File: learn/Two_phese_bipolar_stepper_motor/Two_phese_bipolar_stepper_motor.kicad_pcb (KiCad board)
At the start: 2 copper layers, 73.7 x 81 mm, 25 parts, among them J1 Screw_Terminal_01x02, J2 Screw_Terminal_01x02, J3 Screw_Terminal_01x12, J4 Screw_Terminal_01x04, U1 L297, U2 L298N

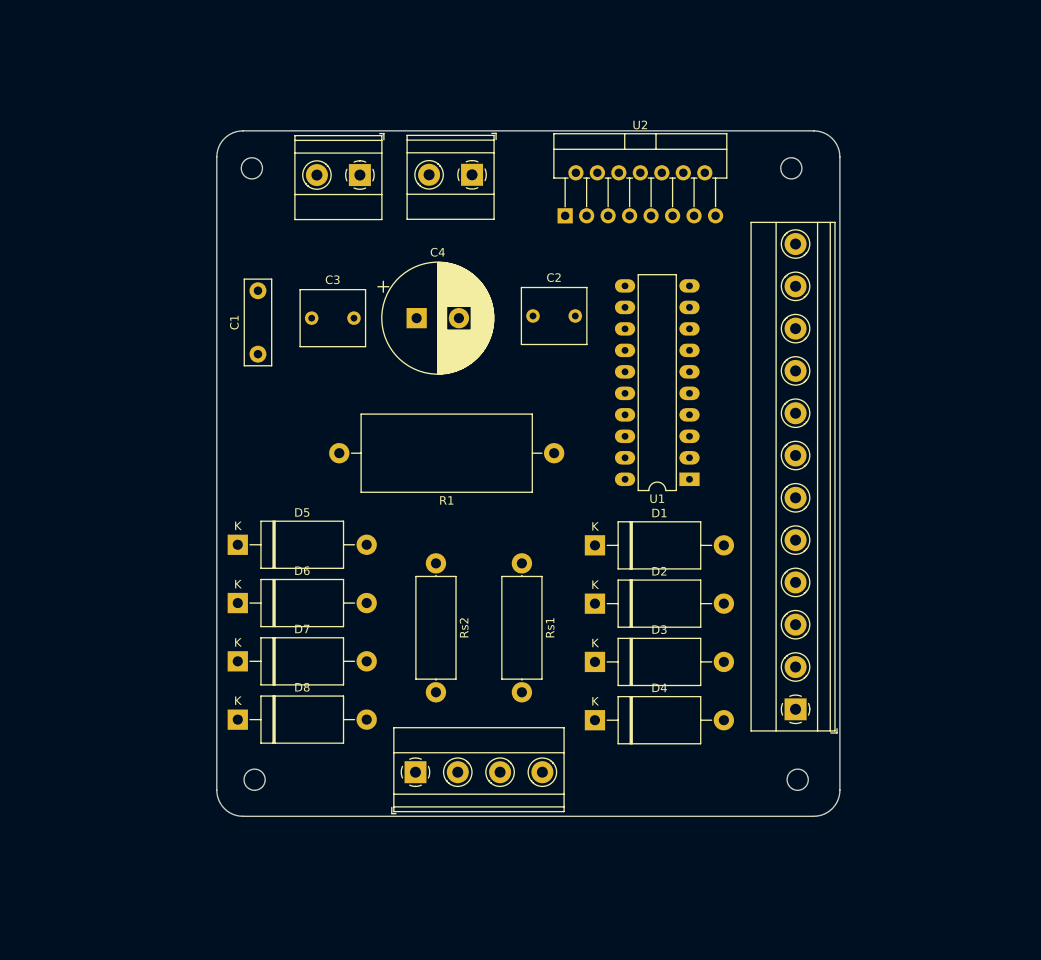
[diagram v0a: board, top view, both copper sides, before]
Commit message: Two_phase: print the wire
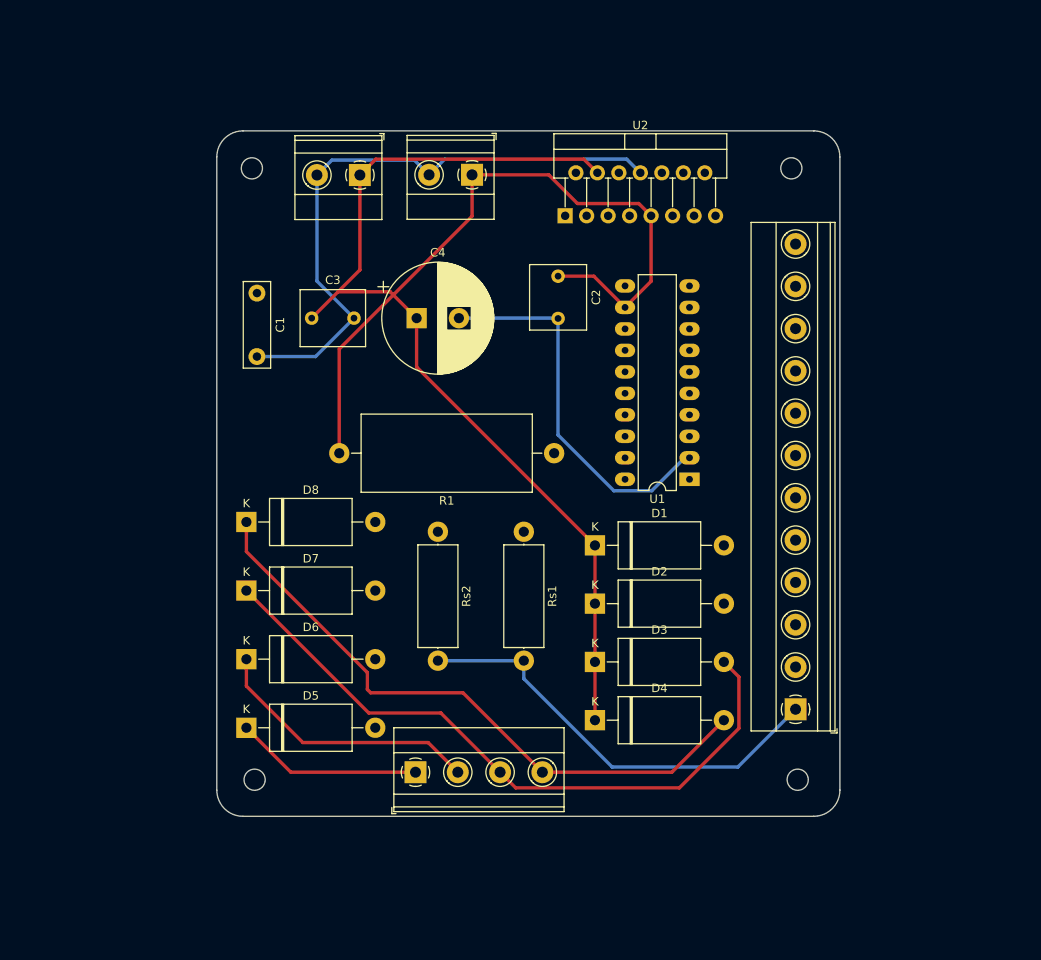
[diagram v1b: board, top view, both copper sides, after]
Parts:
- moved D8 23.4 mm to (116.5, 98.6)
- moved D5 21.7 mm to (116.5, 122.9)
- moved D7 8.42 mm to (116.5, 106.7)
- moved C1 7.22 mm to (117.8, 71.5), turned to -90 degrees
- moved D6 6.71 mm to (116.5, 114.8)
- moved C2 5.56 mm to (153.4, 69.5), turned to -90 degrees
- moved Rs2 3.74 mm to (139.2, 99.7)
- moved Rs1 3.74 mm to (149.3, 99.7)
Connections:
- C2 pad 1: VSS -> VS
- J2 pad 1: VSS -> VS
- R1 pad 2: VSS -> VS
- U1 pad 12: VSS -> VS
- U2 pad 9: VSS -> VS
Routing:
- net VS: track 0.00 -> 199.8 mm
- net GND: track 0.00 -> 170.7 mm
- net Net-(D3-A): track 0.00 -> 79.4 mm
- net Net-(D4-A): track 0.00 -> 74.5 mm
- net Net-(D2-A): track 0.00 -> 32.4 mm
- net Net-(D1-A): track 0.00 -> 22.2 mm

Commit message: two_phase: made pcb
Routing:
- net /OSC: track 0.00 -> 99.6 mm, vias 0 -> 1
- net Net-(D1-A): track 22.2 -> 93.1 mm
- net Net-(D2-A): track 32.4 -> 89.6 mm
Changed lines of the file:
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@@
   (gr_line (start 113.029957 55.410043) (end 113.029957 130.26)
     (stroke (width 0.1) (type default)) (layer "Edge.Cuts"))
+  (segment (start 128.2 93.975) (end 146.875 93.975) (width 0.4) (layer "F.Cu") (net 1))
+  (segment (start 117.775 71.5) (end 116.225 73.05) (width 0.4) (layer "F.Cu") (net 1))
+  (segment (start 116.225 73.05) (end 116.225 82) (width 0.4) (layer "F.Cu") (net 1))
+  (segment (start 152.908 90.424) (end 159.982 83.35) (width 0.4) (layer "F.Cu") (net 1))
+  (segment (start 174.325 68.575) (end 167.825 68.575) (width 0.4) (layer "F.Cu") (net 1))
+  (segment (start 163.04 81.6) (end 161.29 83.35) (width 0.4) (layer "F.Cu") (net 1))
+  (segment (start 167.825 68.575) (end 163.04 73.36) (width 0.4) (layer "F.Cu") (net 1))
+  (segment (start 163.04 73.36) (end 163.04 81.6) (width 0.4) (layer "F.Cu") (net 1))
+  (segment (start 181.45 75.7) (end 174.325 68.575) (width 0.4) (layer "F.Cu") (net 1))
+  (segment (start 159.982 83.35) (end 161.29 83.35) (width 0.4) (layer "F.Cu") (net 1))
+  (segment (start 116.225 82) (end 128.2 93.975) (width 0.4) (layer "F.Cu") (net 1))
+  (via (at 146.875 93.975) (size 0.8) (drill 0.4) (layers "F.Cu" "B.Cu") (net 1))
+  (segment (start 149.357 93.975) (end 152.908 90.424) (width 0.4) (layer "B.Cu") (net 1))
+  (segment (start 146.875 93.975) (end 149.357 93.975) (width 0.4) (layer "B.Cu") (net 1))
   (segment (start 159.769 127.525) (end 174.625 127.525) (width 0.4) (layer "B.Cu") (net 2))
   (segment (start 141.652 74.46) (end 153.335 74.46) (width 0.4) (layer "B.Cu") (net 2))
@@
   (segment (start 143.205 62.410189) (end 127.508 78.107189) (width 0.4) (layer "F.Cu") (net 3))
   (segment (start 121.778666 128.137) (end 116.525 122.883334) (width 0.4) (layer "F.Cu") (net 4))
+  (segment (start 176.925 125.73566) (end 176.925 105.271) (width 0.4) (layer "F.Cu") (net 4))
+  (segment (start 140.756 132.375) (end 170.28566 132.375) (width 0.4) (layer "F.Cu") (net 4))
+  (segment (start 170.28566 132.375) (end 176.925 125.73566) (width 0.4) (layer "F.Cu") (net 4))
+  (segment (start 136.518 128.137) (end 140.756 132.375) (width 0.4) (layer "F.Cu") (net 4))
+  (segment (start 176.925 105.271) (end 172.974 101.32) (width 0.4) (layer "F.Cu") (net 4))
   (segment (start 136.518 128.137) (end 121.778666 128.137) (width 0.4) (layer "F.Cu") (net 4))
   (segment (start 138.014334 124.633334) (end 123.208334 124.633334) (width 0.4) (layer "F.Cu") (net 5))
+  (segment (start 169.975 131.625) (end 145.006 131.625) (width 0.4) (layer "F.Cu") (net 5))
+  (segment (start 172.974 108.21) (end 176.175 111.411) (width 0.4) (layer "F.Cu") (net 5))
   (segment (start 116.525 117.95) (end 116.525 114.775) (width 0.4) (layer "F.Cu") (net 5))
   (segment (start 141.518 128.137) (end 138.014334 124.633334) (width 0.4) (layer "F.Cu") (net 5))
+  (segment (start 176.175 111.411) (end 176.175 125.425) (width 0.4) (layer "F.Cu") (net 5))
+  (segment (start 145.006 131.625) (end 141.518 128.137) (width 0.4) (layer "F.Cu") (net 5))
+  (segment (start 176.175 125.425) (end 169.975 131.625) (width 0.4) (layer "F.Cu") (net 5))
   (segment (start 123.208334 124.633334) (end 116.525 117.95) (width 0.4) (layer "F.Cu") (net 5))
   (segment (start 167.713 129.987) (end 174.75 122.95) (width 0.4) (layer "F.Cu") (net 6))

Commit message: two_phase: made a pcb
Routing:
- net Net-(D3-A): track 79.4 -> 166.0 mm, vias 0 -> 1
- net Net-(D2-A): track 89.6 -> 149.7 mm
- net /Rs2: track 0.00 -> 34.3 mm, vias 0 -> 1
- net /Rs1: track 0.00 -> 30.6 mm, vias 0 -> 1
- net GND: track 170.7 -> 184.6 mm
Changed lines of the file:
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@@
   (segment (start 159.769 127.525) (end 174.625 127.525) (width 0.4) (layer "B.Cu") (net 2))
   (segment (start 141.652 74.46) (end 153.335 74.46) (width 0.4) (layer "B.Cu") (net 2))
+  (segment (start 130.996 72.71) (end 139.902 72.71) (width 0.4) (layer "B.Cu") (net 2))
   (segment (start 136.39 55.78) (end 126.63 55.78) (width 0.4) (layer "B.Cu") (net 2))
   (segment (start 161.485 55.665) (end 163.1 57.28) (width 0.4) (layer "B.Cu") (net 2))
@@
   (segment (start 149.325 117.081) (end 159.769 127.525) (width 0.4) (layer "B.Cu") (net 2))
   (segment (start 168.35 90.97) (end 168.91 90.97) (width 0.4) (layer "B.Cu") (net 2))
+  (segment (start 139.902 72.71) (end 141.652 74.46) (width 0.4) (layer "B.Cu") (net 2))
   (segment (start 159.96 94.86) (end 164.46 94.86) (width 0.4) (layer "B.Cu") (net 2))
   (segment (start 138.125 57.515) (end 136.39 55.78) (width 0.4) (layer "B.Cu") (net 2))
@@
   (segment (start 129.246 74.46) (end 124.706 79) (width 0.4) (layer "B.Cu") (net 2))
   (segment (start 126.63 55.78) (end 124.865 57.545) (width 0.4) (layer "B.Cu") (net 2))
+  (segment (start 129.246 74.46) (end 130.996 72.71) (width 0.4) (layer "B.Cu") (net 2))
   (segment (start 127.508 78.107189) (end 127.508 90.424) (width 0.4) (layer "F.Cu") (net 3))
   (segment (start 131.825 55.665) (end 156.405 55.665) (width 0.4) (layer "F.Cu") (net 3))
@@
   (segment (start 138.014334 124.633334) (end 123.208334 124.633334) (width 0.4) (layer "F.Cu") (net 5))
   (segment (start 169.975 131.625) (end 145.006 131.625) (width 0.4) (layer "F.Cu") (net 5))
+  (segment (start 151.158 91.383) (end 151.158 69.67139) (width 0.4) (layer "F.Cu") (net 5))
+  (segment (start 159.914 95.15) (end 154.925 95.15) (width 0.4) (layer "F.Cu") (net 5))
+  (segment (start 172.974 108.21) (end 159.914 95.15) (width 0.4) (layer "F.Cu") (net 5))
+  (segment (start 154.925 95.15) (end 151.158 91.383) (width 0.4) (layer "F.Cu") (net 5))
+  (segment (start 151.158 69.67139) (end 156.75 64.07939) (width 0.4) (layer "F.Cu") (net 5))
   (segment (start 172.974 108.21) (end 176.175 111.411) (width 0.4) (layer "F.Cu") (net 5))
   (segment (start 116.525 117.95) (end 116.525 114.775) (width 0.4) (layer "F.Cu") (net 5))
   (segment (start 141.518 128.137) (end 138.014334 124.633334) (width 0.4) (layer "F.Cu") (net 5))
   (segment (start 176.175 111.411) (end 176.175 125.425) (width 0.4) (layer "F.Cu") (net 5))
+  (segment (start 156.75 64.07939) (end 156.75 62.36) (width 0.4) (layer "F.Cu") (net 5))
   (segment (start 145.006 131.625) (end 141.518 128.137) (width 0.4) (layer "F.Cu") (net 5))
   (segment (start 176.175 125.425) (end 169.975 131.625) (width 0.4) (layer "F.Cu") (net 5))
@@
   (segment (start 167.713 129.987) (end 174.75 122.95) (width 0.4) (layer "F.Cu") (net 6))
   (segment (start 146.518 128.137) (end 139.514334 121.133334) (width 0.4) (layer "F.Cu") (net 6))
+  (segment (start 172.974 115.1) (end 172.974 111.299) (width 0.4) (layer "F.Cu") (net 6))
   (segment (start 148.368 129.987) (end 167.713 129.987) (width 0.4) (layer "F.Cu") (net 6))
+  (segment (start 150.25 91.53566) (end 150.25 60.05) (width 0.4) (layer "F.Cu") (net 6))
   (segment (start 146.518 128.137) (end 148.368 129.987) (width 0.4) (layer "F.Cu") (net 6))
   (segment (start 174.75 122.95) (end 174.75 116.876) (width 0.4) (layer "F.Cu") (net 6))
   (segment (start 139.514334 121.133334) (end 130.991667 121.133334) (width 0.4) (layer "F.Cu") (net 6))
+  (segment (start 154.61434 95.9) (end 150.25 91.53566) (width 0.4) (layer "F.Cu") (net 6))
+  (segment (start 157.575 95.9) (end 154.61434 95.9) (width 0.4) (layer "F.Cu") (net 6))
+  (segment (start 150.25 60.05) (end 150.55 59.75) (width 0.4) (layer "F.Cu") (net 6))
+  (segment (start 172.974 111.299) (end 157.575 95.9) (width 0.4) (layer "F.Cu") (net 6))
   (segment (start 174.75 116.876) (end 172.974 115.1) (width 0.4) (layer "F.Cu") (net 6))
   (segment (start 130.991667 121.133334) (end 116.525 106.666667) (width 0.4) (layer "F.Cu") (net 6))
+  (via (at 150.55 59.75) (size 0.8) (drill 0.4) (layers "F.Cu" "B.Cu") (net 6))
+  (segment (start 150.55 59.75) (end 166.84 59.75) (width 0.4) (layer "B.Cu") (net 6))
+  (segment (start 166.84 59.75) (end 169.45 62.36) (width 0.4) (layer "B.Cu") (net 6))
   (segment (start 130.825 118.35) (end 130.825 116.35) (width 0.4) (layer "F.Cu") (net 7))
   (segment (start 142.131 118.75) (end 131.225 118.75) (width 0.4) (layer "F.Cu") (net 7))
@@
   (segment (start 130.825 116.35) (end 116.525 102.05) (width 0.4) (layer "F.Cu") (net 7))
   (segment (start 131.225 118.75) (end 130.825 118.35) (width 0.4) (layer "F.Cu") (net 7))
+  (segment (start 158.855 78.27) (end 161.29 78.27) (width 0.4) (layer "F.Cu") (net 18))
+  (segment (start 152.375 84.75) (end 158.855 78.27) (width 0.4) (layer "F.Cu") (net 18))
+  (via (at 152.375 84.75) (size 0.8) (drill 0.4) (layers "F.Cu" "B.Cu") (net 18))
+  (segment (start 149.325 99.71) (end 145.925 96.31) (width 0.4) (layer "B.Cu") (net 18))
+  (segment (start 145.925 96.31) (end 145.925 91.2) (width 0.4) (layer "B.Cu") (net 18))
+  (segment (start 145.925 91.2) (end 152.375 84.75) (width 0.4) (layer "B.Cu") (net 18))
+  (segment (start 159.295 75.73) (end 161.29 75.73) (width 0.4) (layer "F.Cu") (net 19))
+  (segment (start 152.325 82.7) (end 159.295 75.73) (width 0.4) (layer "F.Cu") (net 19))
+  (via (at 152.325 82.7) (size 0.8) (drill 0.4) (layers "F.Cu" "B.Cu") (net 19))
+  (segment (start 139.165 95.86) (end 152.325 82.7) (width 0.4) (layer "B.Cu") (net 19))
+  (segment (start 139.165 99.71) (end 139.165 95.86) (width 0.4) (layer "B.Cu") (net 19))
 )

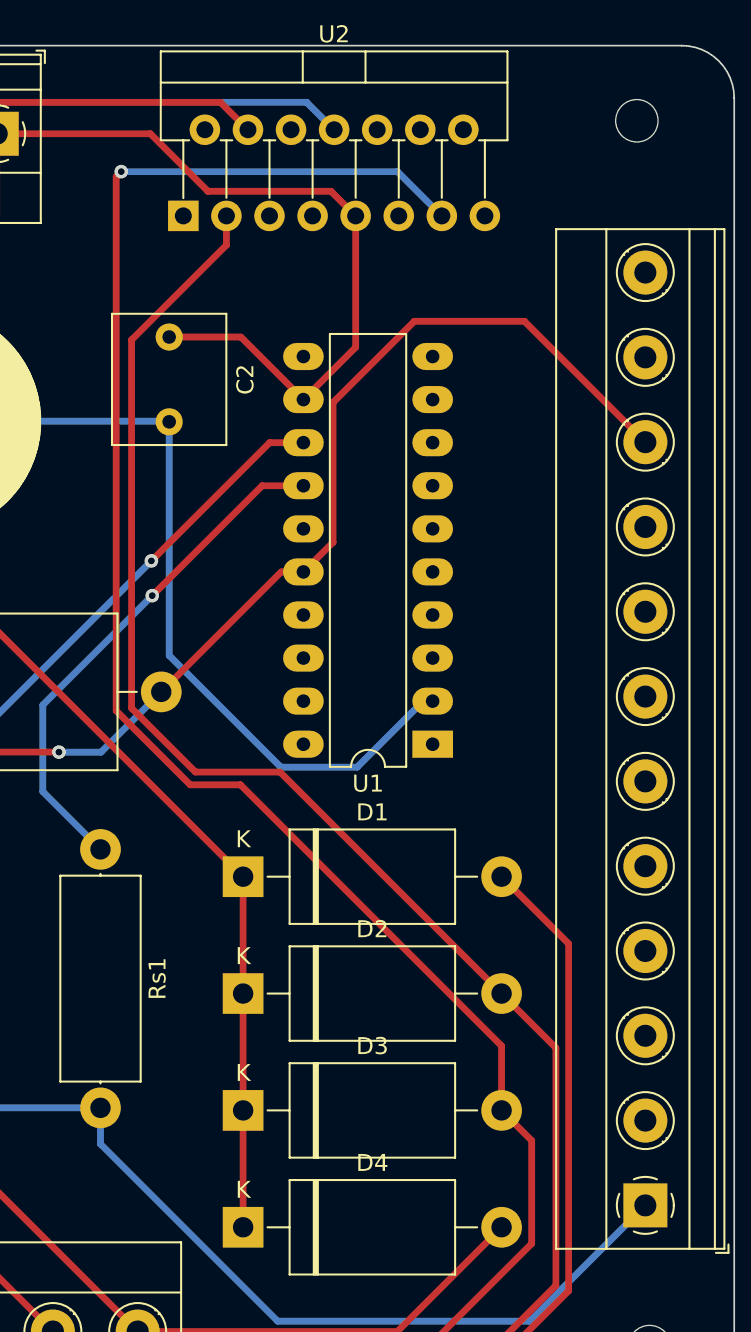
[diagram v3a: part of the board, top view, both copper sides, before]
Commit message: txo_phase: made pcb
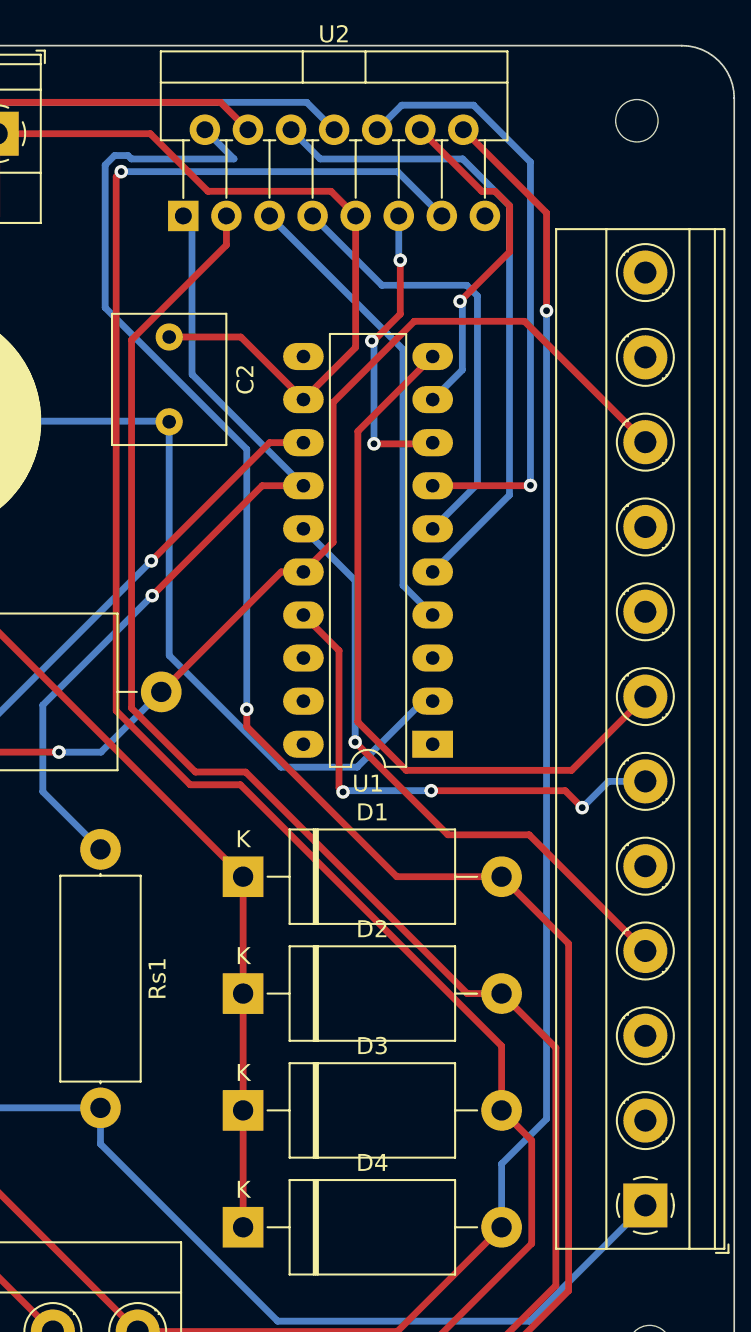
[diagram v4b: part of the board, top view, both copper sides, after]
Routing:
- net Net-(D4-A): track 74.5 -> 142.3 mm, vias 0 -> 1
- net Net-(D1-A): track 93.1 -> 158.7 mm, vias 0 -> 1
- net /ENA: track 0.00 -> 43.3 mm
- net Net-(U1-INH1): track 0.00 -> 38.2 mm
- net /Vref: track 0.00 -> 36.0 mm, vias 0 -> 1
- net Net-(U1-C): track 0.00 -> 35.9 mm, vias 0 -> 1
- net /CW: track 0.00 -> 30.3 mm, vias 0 -> 3
- net Net-(U1-A): track 0.00 -> 27.5 mm
- net Net-(U1-B): track 0.00 -> 26.5 mm
- net Net-(U1-D): track 0.00 -> 20.5 mm, vias 0 -> 1
- net /Rs1: track 30.6 -> 49.5 mm
- net Net-(U1-INH2): track 0.00 -> 17.9 mm, vias 0 -> 3
